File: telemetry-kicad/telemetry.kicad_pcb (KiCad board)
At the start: 4 copper layers, 80 x 80 mm, 126 parts, among them J1 2601-1102, J2 RFPC-SMA27-F, J3 TC2030, J4 2601-1102, J5 MOLEX_104031-0811, J6 2601-1102, J7 USB_C_Receptacle_USB2.0_16P, Q1 DMP3099LQ-7, Q2 MMBT3904, SW1 CJS-1200TB1, SW2 CJS-1200TB1, SW3 SW_NRST, SW4 SW_BOOT0, U1 LMR33610ADDAR, U10 LC29HBAMD, U11 USBLC6-2SC6, U12 TXS0108EPW, U2 TPS2121RUXR, U3 ASM330LHHXG1TR, U4 TCAN337, U5 LM2940CT-5.0/LF01, U6 STM32H523RCT7, U7 TCAN337, U8 TLC59108IPWR, U9 TLC59108IPWR, Y1 ABM8AIG-24.000MHz-8-2Z-T

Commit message: Changed to LC29HEAMD for better RTK 10cm -> 1cm. Changed to active antenna, some passives required.
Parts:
- removed U10: LC29HBAMD, telemetry:LC29HBAMD
- removed U12: TXS0108EPW, Package_SO:TSSOP-20_4.4x6.5mm_P0.65mm
- added C39: 100nF, Capacitor_SMD:C_0402_1005Metric_Pad0.74x0.62mm_HandSolder, F.Cu at (37.8, 47.0)
- added C40: 100pF, Capacitor_SMD:C_0402_1005Metric_Pad0.74x0.62mm_HandSolder, F.Cu at (25.9, 28.2)
- added L2: LQW15AN56NG00D, telemetry:LQW15AN56NG00D, F.Cu at (27.2, 25.7)
- added R40: 10, Resistor_SMD:R_0402_1005Metric_Pad0.72x0.64mm_HandSolder, F.Cu at (28.7, 26.4)
- added U13: LC29HEAMD, telemetry:LC29HEAMD, F.Cu at (31.9, 37.4)
- added U14: TXS0104EPW, Package_SO:TSSOP-14_4.4x5mm_P0.65mm, F.Cu at (26.6, 48.5)
- C36: value 1uF -> 100nF
- C38: value 100nF -> 100pF
- D2: value D20V0L1B2LP-7B -> PESD0402-140; footprint telemetry:D20V0L1B2LP-7B -> telemetry:PESD0402-140
- moved D2 80.9 mm to (24.6, 23.9), turned to 0 degrees
- moved C36 24.2 mm to (28.7, 24.6), turned to 0 degrees
- moved C37 22.2 mm to (39.1, 47.0), turned to -90 degrees
- moved C23 13.8 mm to (21.0, 46.0), turned to 0 degrees
- moved R18 8.06 mm to (53.1, 77.1)
- moved R13 8.01 mm to (61.2, 77.1)
- moved R17 5.54 mm to (54.4, 77.1)
- moved R14 5.51 mm to (60.0, 77.1)
- moved C38 4.03 mm to (28.7, 23.6), turned to 0 degrees
- moved C24 3.01 mm to (23.0, 51.5), turned to 180 degrees
- moved R16 2.58 mm to (55.6, 77.1)
- moved R15 2.38 mm to (58.2, 77.1)
- moved J5 0.17 mm to (56.8, 85.5), turned to 180 degrees
- moved C11 0.06 mm to (56.9, 77.1)
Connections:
- C36 pad 1: +3.3V -> Net-(C36-Pad1)
- C38 pad 1: GND -> Net-(C36-Pad1)
- C38 pad 2: +3.3V -> GND
- D2 pad 1: Net-(D2-A1) -> GND
- D2 pad 2: GND -> ANT
- F1 pad 2: Net-(D2-A1) -> Net-(Q1-D)
- Q1 pad 3: Net-(D2-A1) -> Net-(Q1-D)
- R38 pad 1: DSEL_2 -> VDD_EXT
- R38 pad 2: GND -> DSEL_2
- U6 pad 14: MOSI_GNSS -> RXD1_GNSS
- U6 pad 15: MISO_GNSS -> TXD1_GNSS
- U6 pad 16: CLK_GNSS -> unconnected-(U6A-PA2-Pad16)
- U6 pad 17: CS_GNSS -> unconnected-(U6A-PA3-Pad17)
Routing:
- net D2_SD: track 24.2 -> 46.1 mm
- net CS_GNSS: track 19.0 -> 0.00 mm, vias 2 -> 0
- net D3_SD: track 25.6 -> 44.0 mm, vias 2 -> 4
- net TXD1_GNSS: track 0.00 -> 17.8 mm, vias 0 -> 2
- net CLK_GNSS: track 16.5 -> 0.00 mm, vias 2 -> 0
- net RXD1_GNSS: track 0.00 -> 16.1 mm, vias 0 -> 2
- net MISO_GNSS: track 15.5 -> 0.00 mm, vias 2 -> 0
- net MOSI_GNSS: track 14.6 -> 0.00 mm, vias 2 -> 0
- net CMD_SD: track 27.5 -> 41.2 mm, vias 2 -> 4
- net DET_SD: track 28.6 -> 41.1 mm, vias 2 -> 4
- net VDD_EXT: track 32.1 -> 43.1 mm, vias 0 -> 2
- net CLK_SD: track 31.9 -> 41.9 mm, vias 2 -> 4
- net MOSI_GNSS_2V8: track 9.47 -> 0.00 mm
- net RXD1_GNSS_2V8: track 0.00 -> 9.29 mm
- net MISO_GNSS_2V8: track 8.41 -> 0.00 mm
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
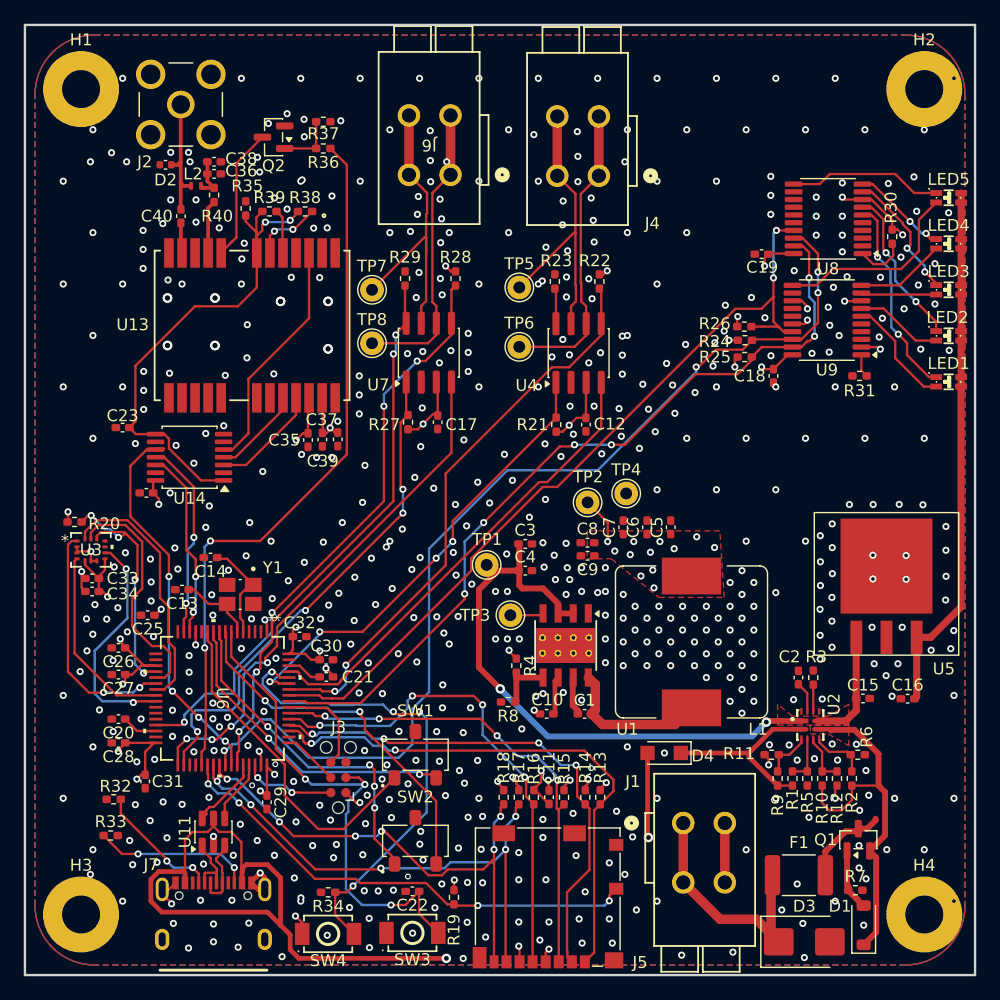
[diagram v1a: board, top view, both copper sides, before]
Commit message: Added two GNSS modules for heading information
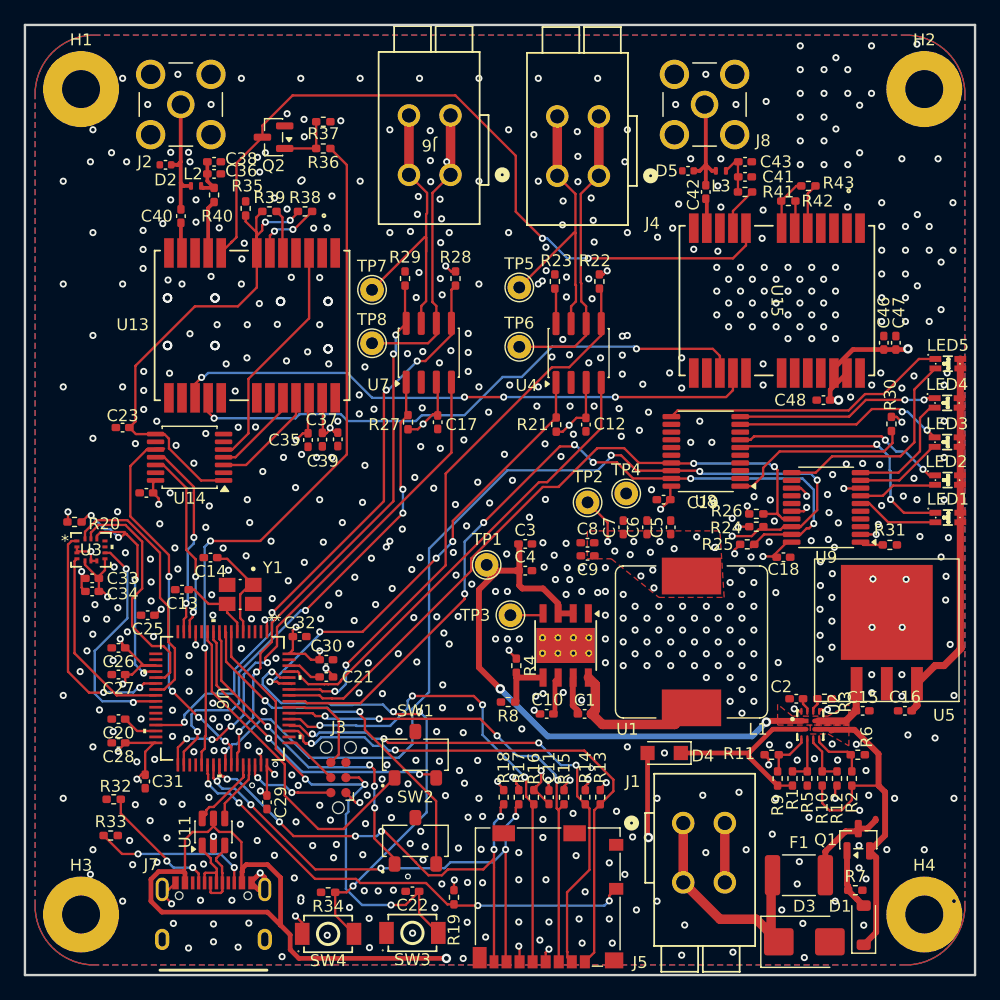
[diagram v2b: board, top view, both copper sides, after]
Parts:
- added C41: 100pF, Capacitor_SMD:C_0402_1005Metric_Pad0.74x0.62mm_HandSolder, F.Cu at (73.4, 24.9)
- added C42: 100pF, Capacitor_SMD:C_0402_1005Metric_Pad0.74x0.62mm_HandSolder, F.Cu at (70.1, 26.2)
- added C43: 100nF, Capacitor_SMD:C_0402_1005Metric_Pad0.74x0.62mm_HandSolder, F.Cu at (73.4, 23.6)
- added C46: 10uF, Capacitor_SMD:C_0402_1005Metric_Pad0.74x0.62mm_HandSolder, F.Cu at (85.1, 38.9)
- added C47: 100nF, Capacitor_SMD:C_0402_1005Metric_Pad0.74x0.62mm_HandSolder, F.Cu at (86.1, 38.9)
- added C48: 1uF, Capacitor_SMD:C_0402_1005Metric_Pad0.74x0.62mm_HandSolder, F.Cu at (80.0, 43.7)
- added D5: PESD0402-140, telemetry:PESD0402-140, F.Cu at (68.6, 24.4)
- added J8: RFPC-SMA27-F, telemetry:RFPC-SMA27-F, F.Cu at (70.0, 18.8)
- added L3: LQW15AN56NG00D, telemetry:LQW15AN56NG00D, F.Cu at (71.4, 24.4)
- added R41: 10, Resistor_SMD:R_0402_1005Metric_Pad0.72x0.64mm_HandSolder, F.Cu at (73.4, 26.2)
- added R42: 39k, Resistor_SMD:R_0402_1005Metric_Pad0.72x0.64mm_HandSolder, F.Cu at (77.1, 26.9)
- added R43: 39k, Resistor_SMD:R_0402_1005Metric_Pad0.72x0.64mm_HandSolder, F.Cu at (78.7, 25.7)
- added U15: LC29HEAMD, telemetry:LC29HEAMD, F.Cu at (76.1, 35.3)
- moved C19 22.3 mm to (66.5, 52.1)
- moved U8 22.1 mm to (70.1, 48.0)
- moved R26 15.8 mm to (74.4, 53.3)
- moved R25 15.8 mm to (73.6, 55.8)
- moved R30 15.8 mm to (85.7, 45.7)
- moved U9 15.8 mm to (80.2, 52.7)
- moved R24 15.7 mm to (74.4, 54.3)
- moved C18 15.3 mm to (76.6, 56.9), turned to 180 degrees
- moved R31 14.5 mm to (85.6, 55.9), turned to 180 degrees
- moved LED5 14.0 mm to (90.5, 40.6)
- moved LED4 13.4 mm to (90.4, 43.9)
- moved LED3 12.8 mm to (90.4, 47.2)
- moved LED2 12.1 mm to (90.5, 50.4)
- moved LED1 11.4 mm to (90.5, 53.6)
- moved U5 3.90 mm to (85.3, 62.6)
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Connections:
- net ANT renamed ANT1
- net ANT_ON renamed ANT_ON_1
- net DSEL_1 renamed DSEL_1_1
- net DSEL_2 renamed DSEL_2_1
- net RF_IN renamed RF_IN_1
- net RXD1_GNSS_2V8 renamed RXD1_GNSS_2V8_1
- net TIMERIN_GNSS_2V8 renamed TIMERIN_GNSS_2V8_1
- net TXD1_GNSS_2V8 renamed TXD1_GNSS_2V8_1
- net VDD_EXT renamed VDD_EXT_1
- net VDD_RF renamed VDD_RF_1
- U13 pad 15: unconnected-(U13-TXD2-Pad15) -> RXD2_GNSS_2V8_2
- U13 pad 16: unconnected-(U13-RXD2-Pad16) -> TXD2_GNSS_2V8_2
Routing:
- net GNSS_RESET_N: track 11.3 -> 64.4 mm, vias 0 -> 2
- net RXD2_GNSS_2V8_2: track 0.00 -> 49.6 mm, vias 0 -> 4
- net TXD2_GNSS_2V8_2: track 0.00 -> 49.3 mm, vias 0 -> 2
- net +5V: track 44.9 -> 31.8 mm
- net Net-(U8-REXT): track 4.29 -> 15.7 mm
- net RST_LED: track 69.1 -> 57.8 mm
- net LED9: track 13.0 -> 24.2 mm
- net +3.3V: track 89.8 -> 99.2 mm, vias 49 -> 52
- net ANT2: track 0.00 -> 9.12 mm
- net LED8: track 8.32 -> 17.0 mm
- net LED7: track 11.1 -> 18.2 mm
- net V_IN: track 61.2 -> 56.0 mm
- net LED6: track 13.4 -> 18.2 mm
- net VDD_EXT_2: track 0.00 -> 4.49 mm
- net GND: track 35.6 -> 31.3 mm, vias 593 -> 682
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
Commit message: Switched to TC2030 with legs, small fixes. 3D models and LDO changed.
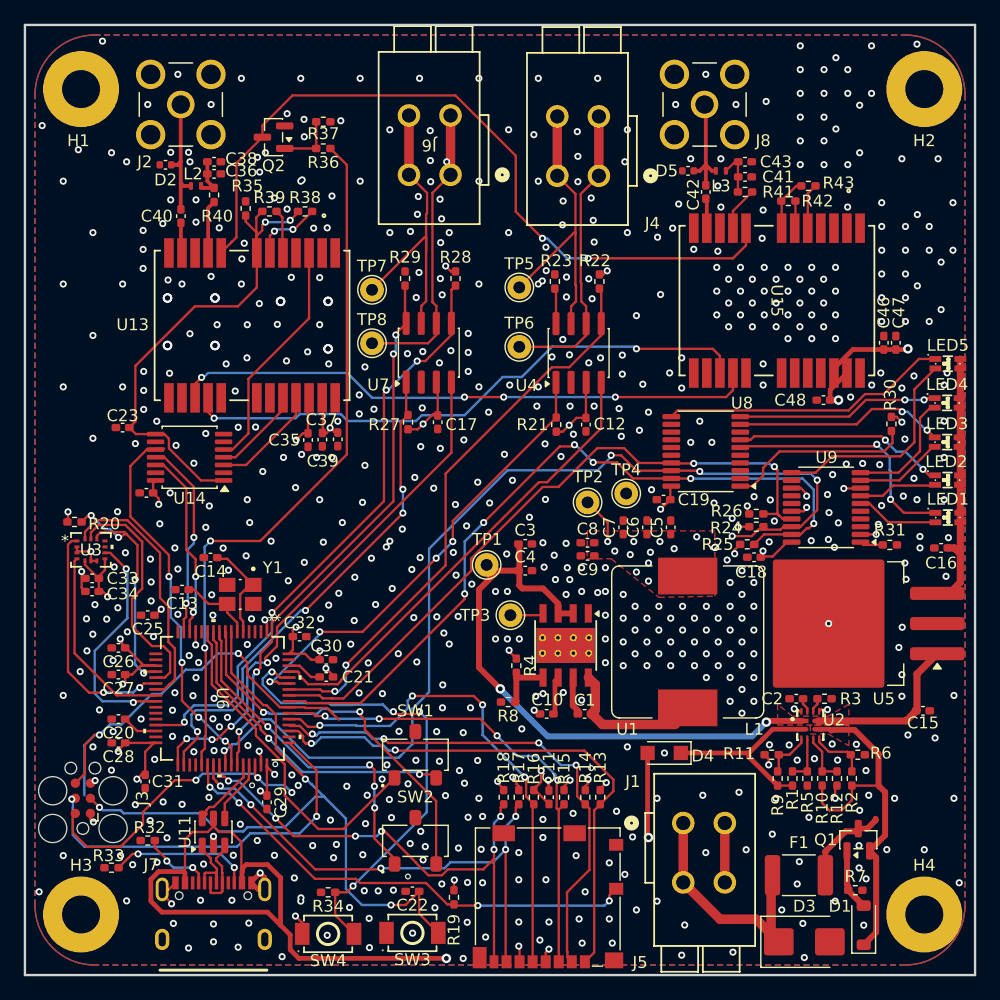
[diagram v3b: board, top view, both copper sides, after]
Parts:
- J3: footprint Connector:Tag-Connect_TC2030-IDC-NL_2x03_P1.27mm_Vertical -> Connector:Tag-Connect_TC2030-IDC-FP_2x03_P1.27mm_Vertical
- U5: footprint telemetry:LM2940CT-5.0-LF01 -> Package_TO_SOT_SMD:TO-263-3_TabPin2
- moved J3 21.6 mm to (17.7, 77.2)
- moved C16 14.1 mm to (89.9, 56.1)
- moved C15 5.08 mm to (88.4, 69.8)
- moved R32 4.50 mm to (23.1, 80.8)
- moved U5 3.40 mm to (81.9, 62.5)
- moved R33 2.71 mm to (20.1, 83.1), turned to 180 degrees
- moved C18 2.47 mm to (74.2, 56.9), turned to 0 degrees
- moved L1 0.32 mm to (68.6, 64.0)
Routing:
- net SWO: track 8.50 -> 36.9 mm, vias 0 -> 2
- net SWCLK: track 4.73 -> 32.6 mm, vias 0 -> 2
- net SWDIO: track 7.94 -> 25.7 mm, vias 2 -> 3
- net NRST: track 42.9 -> 59.3 mm
- net V_IN: track 56.0 -> 65.9 mm
- net +5V: track 31.8 -> 22.4 mm
- net Net-(J7-CC1): track 10.7 -> 6.04 mm
- net Net-(J7-CC2): track 13.4 -> 12.0 mm
- net SW_A: track 31.0 -> 32.0 mm
- net GND: track 31.3 -> 32.1 mm, vias 682 -> 669
